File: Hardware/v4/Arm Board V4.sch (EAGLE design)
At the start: 38 parts, among them IC3 L6206D, P1 STELLARIS-LAUNCHPADSTELLARIS-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, U1 SN74LS241DW, U2 XBEE-1B3

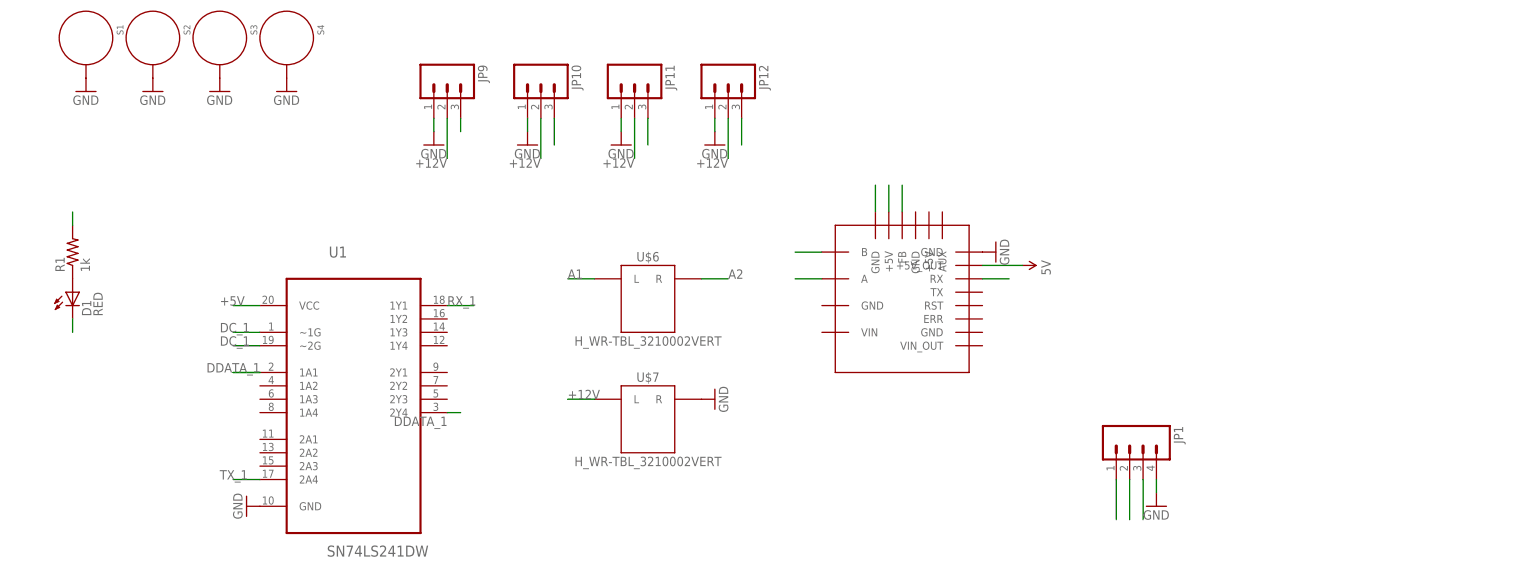
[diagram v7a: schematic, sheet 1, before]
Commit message: cleaned up routes, swapped 603 LEDs for 1206
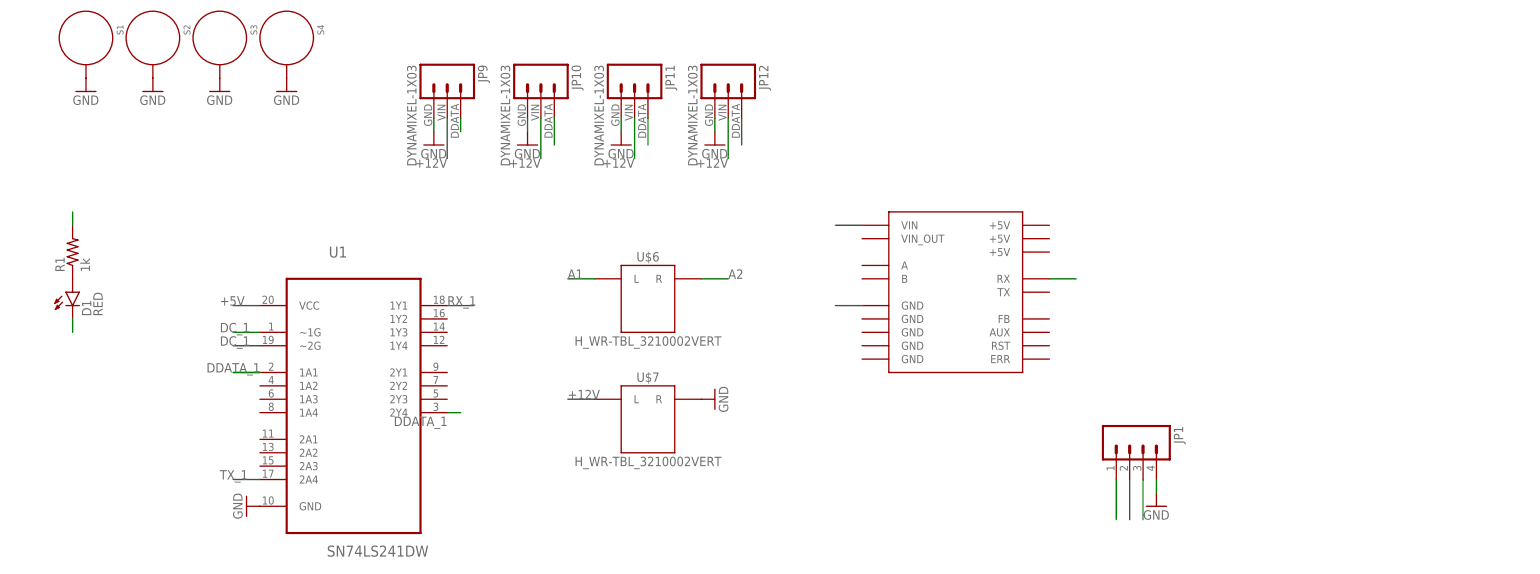
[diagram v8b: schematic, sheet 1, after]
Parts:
- D1, LED1, LED2: device SparkFun-LED:LED-RED0603 -> SparkFun-LED:LED1206
- D2, D3: device SparkFun-DiscreteSemi:DIODE1N4148 -> SparkFun-DiscreteSemi:DIODESOD123
- JP10, JP11, JP12, JP9: value (none) -> DYNAMIXEL-1X03; device SparkFun-Connectors:M03PTH -> MRDT-2015-Arm:DYNAMIXEL-1X03
- LED3: device SparkFun-LED:LED-GREEN0603 -> SparkFun-LED:LED-GREENLARGE
- U$1: device MRDT-RoboticArm:TORXIS_BREAKOUT -> MRDT-2015-Arm:TORXIS_BREAKOUT
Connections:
- removed net N$11: U$1.GND@2
- removed net N$12: U$1.FB
- removed net N$21: U$1.A
- removed net N$22: U$1.B
- removed net N$9: U$1.+5V@1
- net +12V: now also U$1.VIN
- net +5V: no longer U$1.+5V_OUT
- net GND: now also U$1.GND@1; no longer U$1.GND@4
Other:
- moved on the sheet: JP10, JP11, JP12, JP9
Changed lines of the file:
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@@
 <part name="C12" library="SparkFun-Capacitors" deviceset="CAP" device="1206" value=".1uF"/>
 <part name="R12" library="SparkFun-Passives" deviceset="RESISTOR" device="1206" value="1k"/>
-<part name="LED1" library="SparkFun-LED" deviceset="LED-RED" device="0603" value="RED"/>
+<part name="LED1" library="SparkFun-LED" deviceset="LED" device="1206" value="RED"/>
 <part name="GND28" library="SparkFun" deviceset="GND" device=""/>
-<part name="LED2" library="SparkFun-LED" deviceset="LED-RED" device="0603" value="RED"/>
-<part name="LED3" library="SparkFun-LED" deviceset="LED-GREEN" device="0603" value="GREEN"/>
+<part name="LED2" library="SparkFun-LED" deviceset="LED" device="1206" value="RED"/>
+<part name="LED3" library="SparkFun-LED" deviceset="LED-GREEN" device="LARGE" value="GREEN"/>
 <part name="R13" library="SparkFun-Passives" deviceset="RESISTOR" device="1206" value="1k"/>
 <part name="R14" library="SparkFun-Passives" deviceset="RESISTOR" device="1206" value="1k"/>
 <part name="U2" library="SparkFun" deviceset="XBEE-1" device="B3"/>
-<part name="JP9" library="SparkFun-Connectors" deviceset="M03" device="PTH"/>
-<part name="JP10" library="SparkFun-Connectors" deviceset="M03" device="PTH"/>
-<part name="JP11" library="SparkFun-Connectors" deviceset="M03" device="PTH"/>
-<part name="JP12" library="SparkFun-Connectors" deviceset="M03" device="PTH"/>
+<part name="JP9" library="MRDT-2015-Arm" deviceset="DYNAMIXEL-1X03" device=""/>
+<part name="JP10" library="MRDT-2015-Arm" deviceset="DYNAMIXEL-1X03" device=""/>
+<part name="JP11" library="MRDT-2015-Arm" deviceset="DYNAMIXEL-1X03" device=""/>
+<part name="JP12" library="MRDT-2015-Arm" deviceset="DYNAMIXEL-1X03" device=""/>
 <part name="GND1" library="SparkFun-Aesthetics" deviceset="GND" device=""/>
 <part name="GND2" library="SparkFun-Aesthetics" deviceset="GND" device=""/>
@@
 <part name="GND33" library="supply1" deviceset="GND" device=""/>
 <part name="GND34" library="supply1" deviceset="GND" device=""/>
-<part name="U$1" library="MRDT-RoboticArm" deviceset="TORXIS_BREAKOUT" device=""/>
-<part name="GND3" library="SparkFun-Aesthetics" deviceset="GND" device=""/>
+<part name="U$1" library="MRDT-2015-Arm" deviceset="TORXIS_BREAKOUT" device=""/>
 <part name="R1" library="SparkFun-Resistors" deviceset="RESISTOR" device="1206" value="1k"/>
-<part name="D1" library="SparkFun-LED" deviceset="LED-RED" device="0603" value="RED"/>
-<part name="SUPPLY1" library="SparkFun-Aesthetics" deviceset="5V" device=""/>
+<part name="D1" library="SparkFun-LED" deviceset="LED" device="1206" value="RED"/>
 <part name="IC3" library="L6206D" deviceset="L6206" device="D"/>
 <part name="GND17" library="SparkFun-Aesthetics" deviceset="GND" device=""/>
@@
 <part name="C2" library="SparkFun-Passives" deviceset="CAP" device="1206" value="5.6nF"/>
 <part name="GND47" library="SparkFun-Aesthetics" deviceset="GND" device=""/>
-<part name="D2" library="SparkFun-DiscreteSemi" deviceset="DIODE" device="1N4148" value="1N4148"/>
-<part name="D3" library="SparkFun-DiscreteSemi" deviceset="DIODE" device="1N4148" value="1N4148"/>
+<part name="D2" library="SparkFun-DiscreteSemi" deviceset="DIODE" device="SOD123" value="1N4148"/>
+<part name="D3" library="SparkFun-DiscreteSemi" deviceset="DIODE" device="SOD123" value="1N4148"/>
 <part name="C4" library="SparkFun-Passives" deviceset="CAP" device="1206" value="220nF"/>
 <part name="C9" library="SparkFun-Passives" deviceset="CAP" device="1206" value="10nF"/>
@@
 <instance part="JP1" gate="G$1" x="223.52" y="-20.32" rot="R270"/>
 <instance part="GND6" gate="1" x="228.6" y="-30.48"/>
-<instance part="U$1" gate="G$1" x="167.64" y="-2.54"/>
-<instance part="GND3" gate="1" x="198.12" y="17.78" rot="R90"/>
+<instance part="U$1" gate="G$1" x="177.8" y="-5.08"/>
 <instance part="R1" gate="G$1" x="22.86" y="17.78" rot="R90"/>
 <instance part="D1" gate="G$1" x="22.86" y="10.16"/>
-<instance part="SUPPLY1" gate="G$1" x="203.2" y="15.24" rot="R270"/>
 <instance part="U$6" gate="G$1" x="132.08" y="10.16"/>
 </instances>
@@
 </segment>
 <segment>
-<pinref part="U$1" gate="G$1" pin="GND@4"/>
-<pinref part="GND3" gate="1" pin="GND"/>
+<pinref part="U$1" gate="G$1" pin="GND@1"/>
+<wire x1="172.72" y1="7.62" x2="167.64" y2="7.62" width="0.1524" layer="91"/>
 </segment>
 </net>
@@
 <pinref part="JP12" gate="G$1" pin="2"/>
 </segment>
+<segment>
+<pinref part="U$1" gate="G$1" pin="VIN"/>
+<wire x1="172.72" y1="22.86" x2="167.64" y2="22.86" width="0.1524" layer="91"/>
+</segment>
 </net>
 <net name="+5V" class="0">
@@
 <pinref part="R1" gate="G$1" pin="2"/>
 <wire x1="22.86" y1="22.86" x2="22.86" y2="25.4" width="0.1524" layer="91"/>
-</segment>
-<segment>
-<pinref part="U$1" gate="G$1" pin="+5V_OUT"/>
-<pinref part="SUPPLY1" gate="G$1" pin="5V"/>
-<wire x1="203.2" y1="15.24" x2="195.58" y2="15.24" width="0.1524" layer="91"/>
 </segment>
 </net>
@@
 </segment>
 </net>
-<net name="N$9" class="0">
-<segment>
-<pinref part="U$1" gate="G$1" pin="+5V@1"/>
-<wire x1="177.8" y1="25.4" x2="177.8" y2="30.48" width="0.1524" layer="91"/>
-</segment>
-</net>
-<net name="N$11" class="0">
-<segment>
-<pinref part="U$1" gate="G$1" pin="GND@2"/>
-<wire x1="175.26" y1="25.4" x2="175.26" y2="30.48" width="0.1524" layer="91"/>
-</segment>
-</net>
-<net name="N$12" class="0">
-<segment>
-<pinref part="U$1" gate="G$1" pin="FB"/>
-<wire x1="180.34" y1="25.4" x2="180.34" y2="30.48" width="0.1524" layer="91"/>
-</segment>
-</net>
-<net name="RX_7" class="0">
-<segment>
-<pinref part="U$1" gate="G$1" pin="RX"/>
-<wire x1="195.58" y1="12.7" x2="200.66" y2="12.7" width="0.1524" layer="91"/>
-</segment>
-</net>
-<net name="N$21" class="0">
-<segment>
-<pinref part="U$1" gate="G$1" pin="A"/>
-<wire x1="165.1" y1="12.7" x2="160.02" y2="12.7" width="0.1524" layer="91"/>
-</segment>
-</net>
-<net name="N$22" class="0">
-<segment>
-<pinref part="U$1" gate="G$1" pin="B"/>
-<wire x1="165.1" y1="17.78" x2="160.02" y2="17.78" width="0.1524" layer="91"/>
-</segment>
-</net>
 <net name="N$13" class="0">
 <segment>
@@
 </segment>
 </net>
+<net name="RX_7" class="0">
+<segment>
+<pinref part="U$1" gate="G$1" pin="RX"/>
+<wire x1="208.28" y1="12.7" x2="213.36" y2="12.7" width="0.1524" layer="91"/>
+</segment>
+</net>
